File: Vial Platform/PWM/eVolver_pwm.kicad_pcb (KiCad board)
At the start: 4 copper layers, 33 x 66 mm, 66 parts, among them P1 CONN_01X25_1, P2 CONN_01X25_2, P3 CONN_01X10, P4 CONN_01X10, Q1 AO3422, Q10 AO3422, Q11 AO3422, Q12 AO3422, Q13 AO3422, Q14 AO3422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

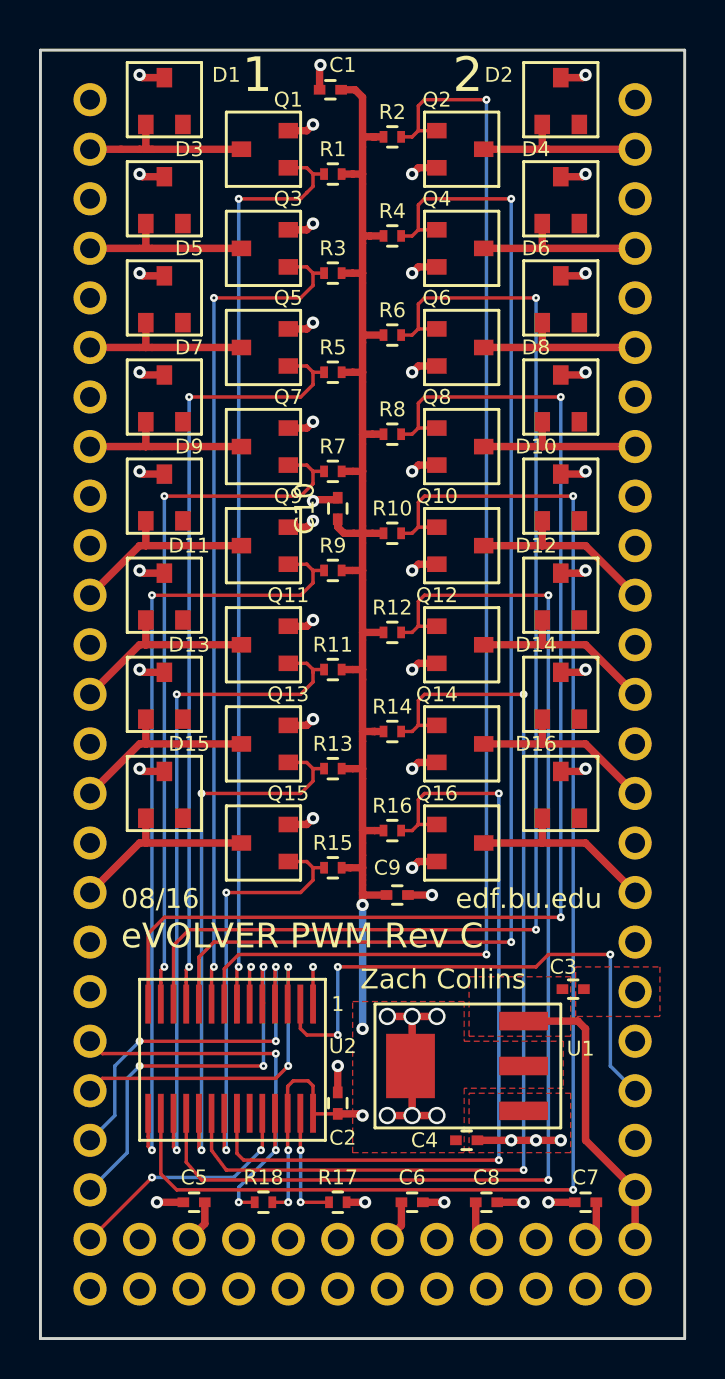
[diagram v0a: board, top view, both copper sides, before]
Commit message: Modified PWM for new  32-VQFN footprint
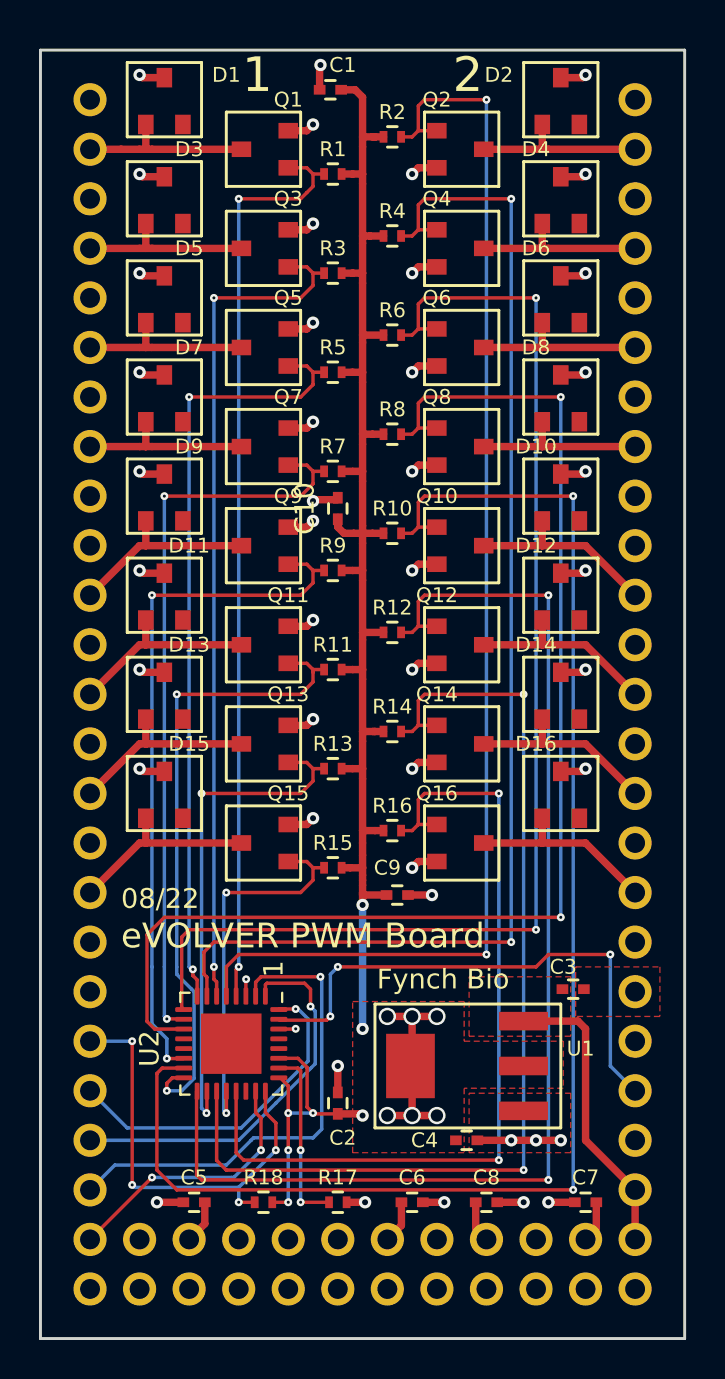
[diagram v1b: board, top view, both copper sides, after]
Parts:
- U2: value TLC5940PWP -> TLC5940RHBR; footprint mods:TLC5940PWP -> mods:TLC5940RHBR
- moved U2 0.64 mm to (163.4, 122.0), turned to -90 degrees
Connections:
- P2 pad 20: (no net) -> unconnected-(P2-Pad20)
- P2 pad 22: (no net) -> unconnected-(P2-Pad22)
- U2 pad 1: GND -> /SCLK
- U2 pad 10: /GATE3 -> /GATE6
- U2 pad 11: /GATE4 -> /GATE7
- U2 pad 12: /GATE5 -> (no net)
- U2 pad 13: /GATE6 -> (no net)
- U2 pad 14: /GATE7 -> /GATE8
- U2 pad 15: /GATE8 -> /GATE9
- U2 pad 16: /GATE9 -> /GATE10
- U2 pad 17: /GATE10 -> /GATE11
- U2 pad 18: /GATE11 -> /GATE12
- U2 pad 19: /GATE12 -> /GATE13
- U2 pad 2: /BLANK -> /SIN
- U2 pad 20: /GATE13 -> /GATE14
- U2 pad 21: /GATE14 -> /GATE15
- U2 pad 22: /GATE15 -> unconnected-(U2-Pad22)
- U2 pad 23: (no net) -> /SOUT
- U2 pad 24: /SOUT -> /GSCLK
- U2 pad 25: /GSCLK -> +3V3
- U2 pad 26: +3V3 -> Net-(R17-Pad1)
- U2 pad 27: Net-(R17-Pad1) -> +3V3
- U2 pad 28: +3V3 -> (no net)
- U2 pad 3: /XLAT -> GND
- U2 pad 4: /SCLK -> /GATE0
- U2 pad 5: /SIN -> /GATE1
- U2 pad 6: GND -> /GATE2
- U2 pad 7: /GATE0 -> /GATE3
- U2 pad 8: /GATE1 -> /GATE4
- U2 pad 9: /GATE2 -> /GATE5
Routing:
- net /GATE8: track 41.5 -> 36.1 mm
- net /SIN: track 20.8 -> 25.2 mm, vias 3 -> 1
- net /GATE9: track 71.5 -> 75.1 mm
- net Net-(R17-Pad1): track 6.02 -> 9.37 mm
- net +3V3: track 92.2 -> 95.4 mm, vias 11 -> 13
- net /GATE7: track 62.5 -> 65.4 mm
- net /GATE12: track 28.8 -> 26.2 mm
- net /GATE14: track 22.5 -> 19.8 mm
- net /GATE10: track 35.3 -> 33.1 mm
- net GND: track 41.8 -> 39.7 mm
- net /GSCLK: track 20.9 -> 22.6 mm, vias 3 -> 4
- net /GATE6: track 36.6 -> 38.2 mm
- net /BLANK: track 28.5 -> 27.2 mm
- net /SCLK: track 18.9 -> 20.1 mm, vias 3 -> 1
- net /GATE15: track 41.9 -> 43.1 mm
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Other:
- net class Default removed
- net class Signal removed
- board text added: "08/22"
- board text added: "Fynch Bio"
- board text added: "eVOLVER PWM Board"
- board text removed: "08/16"
- board text removed: "Zach Collins"
- board text removed: "eVOLVER PWM Rev C"
- board text removed: "edf.bu.edu"

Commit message: Modified via sizes and removed unconnected traces
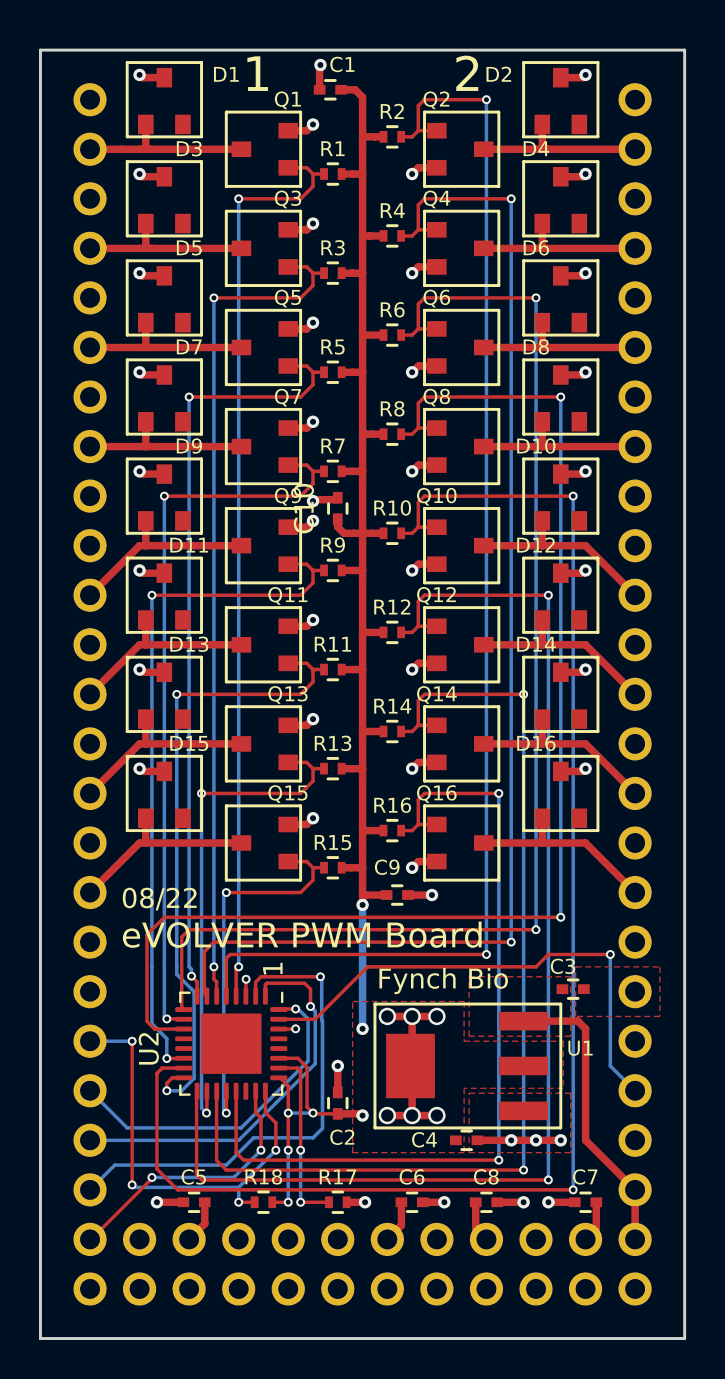
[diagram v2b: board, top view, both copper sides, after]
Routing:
- net /BLANK: track 27.2 -> 25.9 mm, vias 3 -> 1
